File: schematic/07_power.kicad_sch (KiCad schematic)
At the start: 48 parts, among them J101 5V logic test input, U103 MCP100T-450I/TT

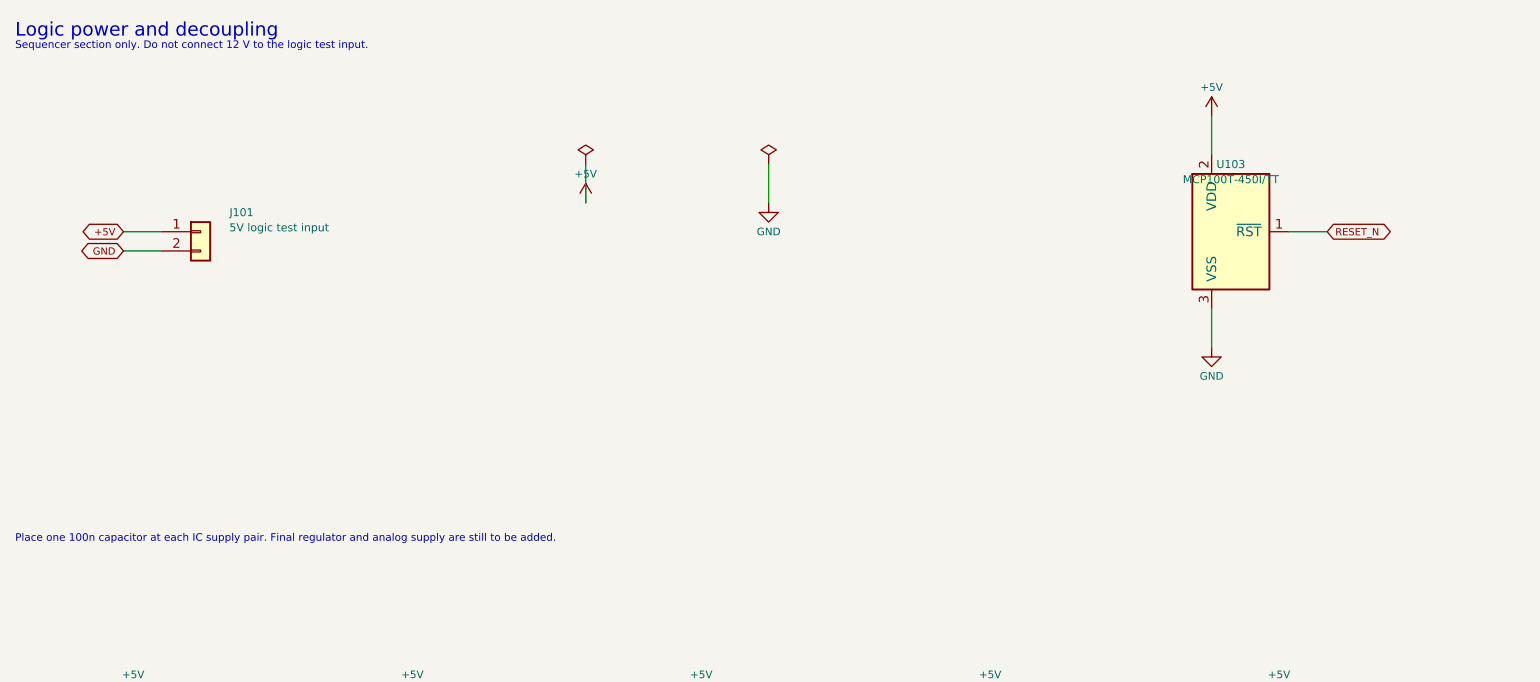
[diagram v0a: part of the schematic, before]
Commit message: add power supply, rail checks and parts list
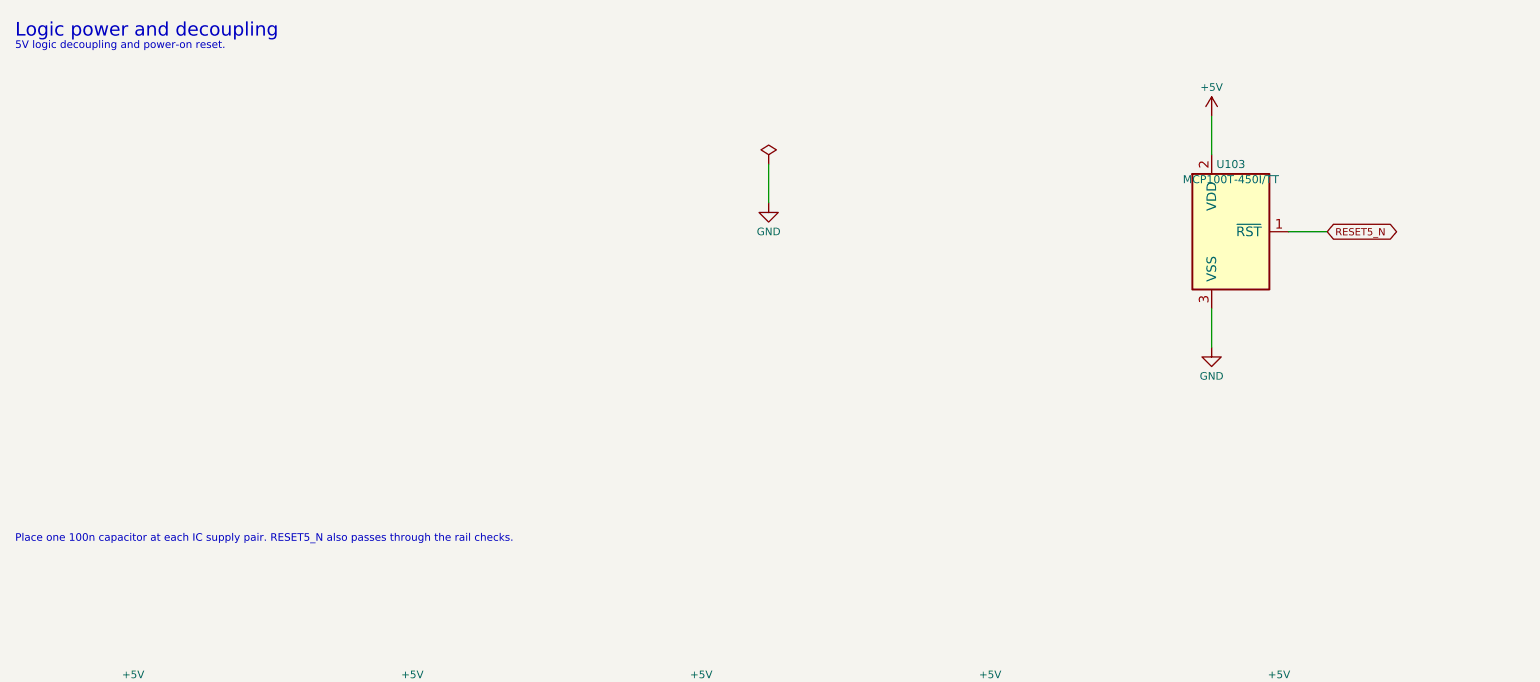
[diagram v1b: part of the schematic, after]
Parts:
- removed J101: 5V logic test input, symbol Connector_Generic:Conn_01x02
- U103: MPN (none) -> MCP100T-450I/TT; Manufacturer (none) -> Microchip; Supplier (none) -> LCSC
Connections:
- net RESET_N renamed RESET5_N
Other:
- note added: "5V logic decoupling and power-on reset."
- note added: "Place one 100n capacitor at each IC supply pair. RESET5_N also passes through the rail checks."
- note removed: "Place one 100n capacitor at each IC supply pair. Final regulator and analog supply are still to be added."
- note removed: "Sequencer section only. Do not connect 12 V to the logic test input."
